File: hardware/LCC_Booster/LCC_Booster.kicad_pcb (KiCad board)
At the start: 2 copper layers, 115 x 100 mm, 101 parts, among them J1 A00-216-262-450, J2 54-00166, J3 Screw_Terminal_01x08, J4 Screw_Terminal_01x02, J5 Screw_Terminal_01x02, Q1 AO3400A, Q2 AO3400A, Q3 AO3400A, Q4 AO3400A, SW1 SW_Push, U1 ACPL-214-500E, U10 7410, U11 DRV8874PWPR, U12 7410, U13 7410, U14 7410, U15 7410, U16 DRV8874PWPR, U17 7410, U18 7410, U19 7410, U2 7410, U20 7410, U21 DRV8874PWPR, U22 MCP2518FD-xQBB, U23 MCP2562-E-SN, U3 7410, U4 7410, U5 7410, U6 DRV8874PWPR, U7 7410, U8 7410, U9 7410, Y1 ECS-400-20-46X

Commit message: Update to hardware v2 and cleanup
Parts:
- removed C36, C38, C41, C42, C43: C100n, Capacitor_SMD:C_0402_1005Metric_Pad0.74x0.62mm_HandSolder
- removed C37: C10u, Capacitor_SMD:C_1206_3216Metric_Pad1.33x1.80mm_HandSolder
- removed C39, C40: C22n, Capacitor_SMD:C_0402_1005Metric_Pad0.74x0.62mm_HandSolder
- removed C44, C45: C22p, Capacitor_SMD:C_0402_1005Metric_Pad0.74x0.62mm_HandSolder
- removed J4, J5: Screw_Terminal_01x02, TerminalBlock_Phoenix:TerminalBlock_Phoenix_MKDS-1,5-2_1x02_P5.00mm_Horizontal
- removed Q1, Q2, Q3, Q4: AO3400A, Package_TO_SOT_SMD:SOT-23
- removed U13, U14, U15, U17, U18, U19, U20: 7410, Package_SO:SOIC-14_3.9x8.7mm_P1.27mm
- removed U16, U21: DRV8874PWPR, DRV8874:PWP0016J_NV
- removed U22: MCP2518FD-xQBB, Package_SO:SOIC-14_3.9x8.7mm_P1.27mm
- removed U23: MCP2562-E-SN, Package_SO:SOIC-8_3.9x4.9mm_P1.27mm
- added JP6: SolderJumper_2_Bridged, Jumper:SolderJumper-2_P1.3mm_Bridged_RoundedPad1.0x1.5mm, F.Cu at (52.6, 74.0)
- added JP7: SolderJumper_2_Bridged, Jumper:SolderJumper-2_P1.3mm_Bridged_RoundedPad1.0x1.5mm, F.Cu at (52.6, 89.0)
- added JP8: SolderJumper_3_Bridged12, Jumper:SolderJumper-3_P1.3mm_Bridged12_RoundedPad1.0x1.5mm_NumberLabels, F.Cu at (91.0, 63.0)
- added JP9: SolderJumper_3_Bridged12, Jumper:SolderJumper-3_P1.3mm_Bridged12_RoundedPad1.0x1.5mm_NumberLabels, F.Cu at (87.0, 63.0)
- C10, C19, C9: value C22n -> C100n
- C11, C18, C25, C4: value C100n -> C10u; footprint Capacitor_SMD:C_0402_1005Metric_Pad0.74x0.62mm_HandSolder -> Capacitor_SMD:C_1206_3216Metric_Pad1.33x1.80mm_HandSolder
- C13, C14, C21, C28, C6: value C100n -> C22n
- C17: value C10u -> C100n; footprint Capacitor_SMD:C_1206_3216Metric_Pad1.33x1.80mm_HandSolder -> Capacitor_SMD:C_0402_1005Metric_Pad0.74x0.62mm_HandSolder
- C27, C7: value C10u -> C22n; footprint Capacitor_SMD:C_1206_3216Metric_Pad1.33x1.80mm_HandSolder -> Capacitor_SMD:C_0402_1005Metric_Pad0.74x0.62mm_HandSolder
- C29, C30: value C22n -> C22p
- J3: footprint TerminalBlock_Phoenix:TerminalBlock_Phoenix_MKDS-1,5-8_1x08_P5.00mm_Horizontal -> TerminalBlock_Phoenix:TerminalBlock_Phoenix_MKDS-1,5-12_1x12_P5.00mm_Horizontal
- JP1, JP3: value SolderJumper_3_Bridged12 -> SolderJumper_2_Open; footprint Jumper:SolderJumper-3_P1.3mm_Bridged12_RoundedPad1.0x1.5mm_NumberLabels -> Jumper:SolderJumper-2_P1.3mm_Open_RoundedPad1.0x1.5mm
- JP2: value SolderJumper_3_Bridged12 -> SolderJumper_2_Open; footprint Jumper:SolderJumper-3_P1.3mm_Bridged12_RoundedPad1.0x1.5mm_NumberLabels -> Jumper:SolderJumper-2_P1.3mm_Bridged_RoundedPad1.0x1.5mm
- JP4: value SolderJumper_3_Bridged12 -> SolderJumper_2_Bridged; footprint Jumper:SolderJumper-3_P1.3mm_Bridged12_RoundedPad1.0x1.5mm_NumberLabels -> Jumper:SolderJumper-2_P1.3mm_Bridged_RoundedPad1.0x1.5mm
- JP5: value SolderJumper_2_Open -> SolderJumper_2_Bridged; footprint Jumper:SolderJumper-2_P1.3mm_Open_RoundedPad1.0x1.5mm -> Jumper:SolderJumper-2_P1.3mm_Bridged_RoundedPad1.0x1.5mm
- U10, U4, U8: value 7410 -> DRV8874PWPR; footprint Package_SO:SOIC-14_3.9x8.7mm_P1.27mm -> DRV8874:PWP0016J_NV
- U11: value DRV8874PWPR -> MCP2518FD-xQBB; footprint DRV8874:PWP0016J_NV -> Package_SO:SOIC-14_3.9x8.7mm_P1.27mm
- U12: value 7410 -> MCP2562-E-SN; footprint Package_SO:SOIC-14_3.9x8.7mm_P1.27mm -> Package_SO:SOIC-8_3.9x4.9mm_P1.27mm
- U2: value 7410 -> ACPL-214-500E; footprint Package_SO:SOIC-14_3.9x8.7mm_P1.27mm -> Package_SO:SOP-4_4.4x2.6mm_P1.27mm
- U3, U5, U7, U9: value 7410 -> SN74HC253DR; footprint Package_SO:SOIC-14_3.9x8.7mm_P1.27mm -> Package_SO:SO-16_3.9x9.9mm_P1.27mm
- moved H2 106.3 mm to (100.0, 30.0)
- moved H4 106.3 mm to (30.0, 110.0)
- moved JP5 75.1 mm to (52.6, 59.0)
- moved U2 72.0 mm to (83.0, 98.0), turned to 90 degrees
- moved C30 65.9 mm to (108.9, 70.3), turned to 90 degrees
- moved U11 63.6 mm to (103.0, 62.0), turned to 90 degrees
- moved C29 61.8 mm to (101.0, 70.3), turned to 90 degrees
- moved JP4 57.9 mm to (52.6, 44.0), turned to 90 degrees
- moved SW1 57.1 mm to (66.5, 36.0), turned to 90 degrees
- moved C32 55.2 mm to (97.0, 59.5), turned to 180 degrees
- moved C31 50.2 mm to (86.5, 75.5), turned to 180 degrees
- moved R10 49.9 mm to (43.7, 87.5), turned to 180 degrees
- moved C33 49.2 mm to (80.5, 72.0), turned to 90 degrees
- moved U1 46.9 mm to (83.0, 85.0)
- moved U9 45.2 mm to (52.7, 94.6), turned to -90 degrees
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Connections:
- A1 pad 1: /dcc_en_D -> /dcc_en_C
- A1 pad 12: /pwm_B -> /pwm_A
- A1 pad 19: /sense_A -> /sense_D
- A1 pad 2: /dcc_en_C -> /dcc_en_D
- A1 pad 20: /sense_B -> /sense_C
- A1 pad 21: /sense_C -> /sense_B
- A1 pad 22: /sense_D -> /sense_A
- A1 pad 25: /dcc_en_A -> /dcc_en_B
- A1 pad 26: /dcc_en_B -> /dcc_en_A
- A1 pad 6: /pwm_A -> /pwm_D
- A1 pad 8: /pwm_D -> /pwm_C
- A1 pad 9: /pwm_C -> /pwm_B
- C10 pad 1: /sense_A -> VTRACK
- C10 pad 2: GND -> Net-(U6-VCP)
- C11 pad 1: IOREF -> VTRACK
- C12 pad 1: IOREF -> VTRACK
- C13 pad 1: IOREF -> Net-(U6-CPH)
- C13 pad 2: GND -> Net-(U6-CPL)
- C14 pad 1: IOREF -> /sense_B
- C16 pad 1: VTRACK -> IOREF
- C16 pad 2: Net-(U11-VCP) -> GND
- C17 pad 2: GND -> Net-(U8-VCP)
- C19 pad 1: Net-(U11-CPH) -> VTRACK
- C19 pad 2: Net-(U11-CPL) -> GND
- C20 pad 1: /sense_B -> Net-(U8-CPH)
- C20 pad 2: GND -> Net-(U8-CPL)
- C21 pad 1: IOREF -> /sense_C
- C24 pad 1: IOREF -> VTRACK
- C24 pad 2: GND -> Net-(U10-VCP)
- C25 pad 1: IOREF -> VTRACK
- C26 pad 2: Net-(U16-VCP) -> GND
- C27 pad 1: VTRACK -> Net-(U10-CPH)
- C27 pad 2: GND -> Net-(U10-CPL)
- C28 pad 1: VTRACK -> /sense_D
- C29 pad 1: Net-(U16-CPH) -> GND
- C29 pad 2: Net-(U16-CPL) -> Net-(U11-OSC2)
- C3 pad 1: IOREF -> VTRACK
- C3 pad 2: GND -> Net-(U4-VCP)
- C30 pad 1: /sense_C -> GND
- C30 pad 2: GND -> Net-(U11-OSC1)
- C33 pad 1: IOREF -> +5V
- C4 pad 1: IOREF -> VTRACK
- C5 pad 1: IOREF -> VTRACK
- C6 pad 1: VTRACK -> Net-(U4-CPH)
- C6 pad 2: Net-(U6-VCP) -> Net-(U4-CPL)
- C7 pad 1: VTRACK -> /sense_A
- C8 pad 1: VTRACK -> IOREF
- C9 pad 1: Net-(U6-CPH) -> IOREF
- C9 pad 2: Net-(U6-CPL) -> GND
- J3 pad 1: /out2_D -> /raw_dcc_n
- J3 pad 2: /out1_D -> /raw_dcc_p
- J3 pad 3: /out2_C -> /out2_D
- J3 pad 4: /out1_C -> /out1_D
- J3 pad 5: /out2_B -> /out2_C
- J3 pad 6: /out1_B -> /out1_C
- J3 pad 7: /out2_A -> /out2_B
- J3 pad 8: /out1_A -> /out1_B
- JP1 pad 1: +5V -> /can_shield
- JP1 pad 2: 3v3_IOREF -> GND
- JP3 pad 1: Net-(JP3-A) -> IOREF
- JP3 pad 2: /cs_canrx -> +5V
- JP4 pad 1: Net-(JP4-A) -> GND
- JP4 pad 2: /int_cantx -> Net-(JP4-B)
- JP5 pad 1: /can_shield -> GND
- JP5 pad 2: GND -> Net-(JP5-B)
- R1 pad 2: Net-(U6-FAULT_N) -> Net-(U4-FAULT_N)
- R10 pad 2: Net-(U21-FAULT_N) -> Net-(U10-FAULT_N)
- R2 pad 2: Net-(Q1-D) -> Net-(JP4-B)
- R3 pad 1: Net-(Q1-D) -> Net-(JP4-B)
- R4 pad 2: Net-(U11-FAULT_N) -> Net-(U6-FAULT_N)
- R5 pad 2: Net-(Q2-D) -> Net-(JP5-B)
- R6 pad 1: Net-(Q2-D) -> Net-(JP5-B)
- R7 pad 2: Net-(U16-FAULT_N) -> Net-(U8-FAULT_N)
- U10 pad 1: Net-(U10-Pad1) -> Net-(U10-EN_IN1)
- U10 pad 10: unconnected-(U10-Pad10) -> /out2_D
- U10 pad 11: unconnected-(U10-Pad11) -> VTRACK
- U10 pad 12: Net-(U11-EN_IN1) -> Net-(U10-VCP)
- U10 pad 13: Net-(U10-Pad13) -> Net-(U10-CPH)
- U10 pad 14: IOREF -> Net-(U10-CPL)
- U10 pad 2: Net-(U10-Pad2) -> Net-(U10-PH_IN2)
- U10 pad 3: Net-(U10-Pad3) -> IOREF
- U10 pad 4: Net-(U10-Pad4) -> Net-(U10-FAULT_N)
- U10 pad 5: Net-(U10-Pad5) -> IOREF
- U10 pad 6: Net-(U11-PH_IN2) -> /sense_D
- U10 pad 8: unconnected-(U10-Pad8) -> /out1_D
- U10 pad 9: unconnected-(U10-Pad9) -> GND
- U11 pad 1: Net-(U11-EN_IN1) -> Net-(JP9-B)
- U11 pad 10: /out2_B -> /sck
- U11 pad 11: VTRACK -> /copi
- U11 pad 12: Net-(U11-VCP) -> /cipo
- U11 pad 13: Net-(U11-CPH) -> Net-(JP8-A)
- U11 pad 14: Net-(U11-CPL) -> IOREF
- U11 pad 2: Net-(U11-PH_IN2) -> Net-(JP8-B)
- U11 pad 3: IOREF -> unconnected-(U11-CLKO/SOF-Pad3)
- U11 pad 4: Net-(U11-FAULT_N) -> Net-(JP9-A)
- U11 pad 5: IOREF -> Net-(U11-OSC2)
- U11 pad 6: /sense_B -> Net-(U11-OSC1)
- U11 pad 8: /out1_B -> unconnected-(U11-~{INT1}/GPIO1-Pad8)
- U11 pad 9: GND -> unconnected-(U11-~{INT0}/GPIO0/XSTBY-Pad9)
- U12 pad 1: /dcc_en_C -> Net-(JP9-B)
- U12 pad 2: /dcc_en_C -> GND
- U12 pad 3: /dir_C -> +5V
- U12 pad 4: /dir_C -> Net-(JP8-B)
- U12 pad 5: /dir_C -> IOREF
- U12 pad 6: Net-(U12-Pad6) -> /can_l
- U12 pad 7: GND -> /can_h
- U12 pad 8: Net-(U12-Pad8) -> GND
- U2 pad 1: /dcc_en_A -> /raw_dcc_n
- U2 pad 2: /dcc_en_A -> GND
- U2 pad 3: /dir_A -> /dcc_n
- U2 pad 4: /dir_A -> IOREF
- U3 pad 1: Net-(U2-Pad8) -> GND
- U3 pad 10: Net-(U2-Pad12) -> GND
- U3 pad 11: Net-(U2-Pad6) -> /pwm_A
- U3 pad 12: Net-(U3-Pad12) -> /dcc_n
- U3 pad 13: /dir_A -> /dcc_p
- U3 pad 14: IOREF -> /dir_A
- U3 pad 3: /dcc_p -> /dcc_n
- U3 pad 4: /dcc_en_A -> /dcc_p
- U3 pad 5: Net-(U2-Pad6) -> GND
- U3 pad 6: Net-(U3-Pad6) -> /pwm_A
- U3 pad 7: GND -> Net-(U3-1Y)
- U3 pad 8: Net-(U3-Pad8) -> GND
- U3 pad 9: /pwm_A -> Net-(U3-2Y)
- U4 pad 1: /dcc_p -> Net-(U3-1Y)
- U4 pad 10: Net-(U2-Pad12) -> /out2_A
- U4 pad 11: /dir_A -> VTRACK
- U4 pad 12: Net-(U4-Pad12) -> Net-(U4-VCP)
- U4 pad 13: /dir_A -> Net-(U4-CPH)
- U4 pad 14: IOREF -> Net-(U4-CPL)
- U4 pad 2: /dcc_en_A -> Net-(U3-2Y)
- U4 pad 3: Net-(U2-Pad8) -> IOREF
- U4 pad 4: /dcc_en_A -> Net-(U4-FAULT_N)
- U4 pad 5: Net-(U2-Pad6) -> IOREF
- U4 pad 6: Net-(U4-Pad6) -> /sense_A
- U4 pad 8: Net-(U4-Pad8) -> /out1_A
- U4 pad 9: /pwm_A -> GND
- U5 pad 1: Net-(U3-Pad12) -> GND
- U5 pad 10: unconnected-(U5-Pad10) -> GND
- U5 pad 11: unconnected-(U5-Pad11) -> /pwm_B
- U5 pad 12: Net-(U6-EN_IN1) -> /dcc_n
- U5 pad 13: Net-(U3-Pad8) -> /dcc_p
- U5 pad 14: IOREF -> /dir_B
- U5 pad 2: Net-(U3-Pad6) -> /dcc_en_B
- U5 pad 3: Net-(U4-Pad12) -> /dcc_n
- U5 pad 4: Net-(U4-Pad6) -> /dcc_p
- U5 pad 5: Net-(U4-Pad8) -> GND
- U5 pad 6: Net-(U6-PH_IN2) -> /pwm_B
- U5 pad 7: GND -> Net-(U5-1Y)
- U5 pad 8: unconnected-(U5-Pad8) -> GND
- U5 pad 9: unconnected-(U5-Pad9) -> Net-(U5-2Y)
- U6 pad 1: Net-(U6-EN_IN1) -> Net-(U5-1Y)
- U6 pad 10: /out2_A -> /out2_B
- U6 pad 2: Net-(U6-PH_IN2) -> Net-(U5-2Y)
- U6 pad 6: /sense_A -> /sense_B
- U6 pad 8: /out1_A -> /out1_B
- U7 pad 1: /dcc_en_B -> GND
- U7 pad 10: /dcc_p -> GND
- U7 pad 11: /dcc_p -> /pwm_C
- U7 pad 12: Net-(U7-Pad12) -> /dcc_n
- U7 pad 13: /dcc_en_B -> /dcc_p
- U7 pad 14: IOREF -> /dir_C
- U7 pad 2: /dcc_en_B -> /dcc_en_C
- U7 pad 3: /dir_B -> /dcc_n
- U7 pad 4: /dir_B -> /dcc_p
- U7 pad 5: /dir_B -> GND
- U7 pad 6: Net-(U7-Pad6) -> /pwm_C
- U7 pad 7: GND -> Net-(U7-1Y)
- U7 pad 8: Net-(U7-Pad8) -> GND
- U7 pad 9: /dcc_p -> Net-(U7-2Y)
- U8 pad 1: Net-(U7-Pad8) -> Net-(U7-1Y)
- U8 pad 10: Net-(U7-Pad12) -> /out2_C
- U8 pad 11: Net-(U7-Pad6) -> VTRACK
- U8 pad 12: Net-(U10-Pad1) -> Net-(U8-VCP)
- U8 pad 13: /dir_B -> Net-(U8-CPH)
- U8 pad 14: IOREF -> Net-(U8-CPL)
- U8 pad 2: /dcc_en_B -> Net-(U7-2Y)
- U8 pad 3: /dcc_p -> IOREF
- U8 pad 4: /dcc_en_B -> Net-(U8-FAULT_N)
- U8 pad 5: Net-(U7-Pad6) -> IOREF
- U8 pad 6: Net-(U10-Pad2) -> /sense_C
- U8 pad 8: Net-(U10-Pad13) -> /out1_C
- U8 pad 9: /pwm_B -> GND
- U9 pad 1: /dcc_p -> GND
- U9 pad 10: Net-(U7-Pad12) -> GND
- U9 pad 11: /dir_B -> /pwm_D
- U9 pad 12: Net-(U10-Pad3) -> /dcc_n
- U9 pad 13: /dir_B -> /dcc_p
- U9 pad 14: IOREF -> /dir_D
- U9 pad 2: /dcc_en_B -> /dcc_en_D
- U9 pad 3: Net-(U7-Pad8) -> /dcc_n
- U9 pad 4: /dcc_en_B -> /dcc_p
- U9 pad 5: Net-(U7-Pad6) -> GND
- U9 pad 6: Net-(U10-Pad4) -> /pwm_D
- U9 pad 7: GND -> Net-(U10-EN_IN1)
- U9 pad 8: Net-(U10-Pad5) -> GND
- U9 pad 9: /pwm_B -> Net-(U10-PH_IN2)
- Y1 pad 1: Net-(U22-OSC1) -> Net-(U11-OSC1)
- Y1 pad 2: Net-(U22-OSC2) -> Net-(U11-OSC2)
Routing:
- net IOREF: track 575.4 -> 267.0 mm, vias 20 -> 18
- net 3v3_IOREF: track 148.3 -> 0.00 mm, vias 4 -> 0
- net /dcc_n: track 0.00 -> 125.4 mm, vias 0 -> 5
- net /raw_dcc_p: track 197.2 -> 100.5 mm
- net /dcc_p: track 240.7 -> 147.6 mm, vias 8 -> 5
- net /sense_D: track 171.2 -> 94.9 mm, vias 3 -> 0
- net GND: track 412.6 -> 350.7 mm, vias 130 -> 66
- net /dir_D: track 114.2 -> 53.9 mm, vias 5 -> 2
- net Net-(U21-FAULT_N): track 59.7 -> 0.00 mm
- net /dcc_en_D: track 96.7 -> 42.9 mm, vias 2 -> 0
- net /sense_C: track 132.0 -> 79.6 mm, vias 2 -> 0
- net Net-(U11-FAULT_N): track 50.0 -> 0.00 mm, vias 2 -> 0
- net +5V: track 108.2 -> 58.6 mm
- net /dcc_en_C: track 79.4 -> 29.8 mm, vias 2 -> 0
- net /sense_A: track 110.1 -> 62.1 mm
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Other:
- board size 115 x 100 mm -> 90 x 100 mm
- board text added: "3.3v"
- board text added: "5v"
- board text added: "Nano V_{IN}"
- board text added: "Reset"
- board text added: "TMRC System 4 Block Card v2"
- board text added: "V_{TRACK}"
- board text removed: "3.3V"
- board text removed: "5V"
- board text removed: "CAN"
- board text removed: "RESET"
- board text removed: "SPI"
- board text removed: "TMRC System 4 Block Card v1.0"
- board text removed: "V_TRACK"

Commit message: Update Schematic
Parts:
- added R13: R1k 2W, Resistor_SMD:R_01005_0402Metric_Pad0.57x0.30mm_HandSolder, F.Cu at (64.8, 98.2)
- added R14: R10k, Resistor_SMD:R_01005_0402Metric_Pad0.57x0.30mm_HandSolder, F.Cu at (85.0, 85.8)
- added R15: R10k, Resistor_SMD:R_01005_0402Metric_Pad0.57x0.30mm_HandSolder, F.Cu at (79.5, 99.2)
- U1, U2: value ACPL-214-500E -> 6N137; footprint Package_SO:SOP-4_4.4x2.6mm_P1.27mm -> Package_DIP:DIP-8_W7.62mm_SMDSocket_SmallPads
- moved U1 17.7 mm to (72.5, 99.2), turned to 0 degrees
- moved U2 14.5 mm to (78.2, 84.2), turned to 0 degrees
- moved C34 4.78 mm to (83.5, 78.2), turned to 0 degrees
- moved C35 2.57 mm to (77.8, 93.2), turned to 0 degrees
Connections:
- C34 pad 1: IOREF -> +5V
- C35 pad 1: IOREF -> +5V
- U1 pad 1: /raw_dcc_p -> unconnected-(U1-NC-Pad1)
- U1 pad 2: GND -> Net-(U1-A)
- U1 pad 3: /dcc_p -> /raw_dcc_n
- U1 pad 4: IOREF -> unconnected-(U1-NC-Pad4)
- U2 pad 1: /raw_dcc_n -> unconnected-(U2-NC-Pad1)
- U2 pad 2: GND -> /raw_dcc_n
- U2 pad 3: /dcc_n -> Net-(U1-A)
- U2 pad 4: IOREF -> unconnected-(U2-NC-Pad4)
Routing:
- net /raw_dcc_n: track 94.8 -> 129.9 mm
- net +5V: track 58.6 -> 89.0 mm
- net GND: track 350.7 -> 379.8 mm
- net Net-(U1-A): track 0.00 -> 22.0 mm
- net /raw_dcc_p: track 100.5 -> 111.5 mm
- net /dcc_n: track 125.4 -> 116.6 mm
- net /dcc_p: track 147.6 -> 152.1 mm, vias 5 -> 6
- net IOREF: track 267.0 -> 271.3 mm
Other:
- board text added: "TMRC System 4 Block Card v3"
- board text removed: "TMRC System 4 Block Card v2"

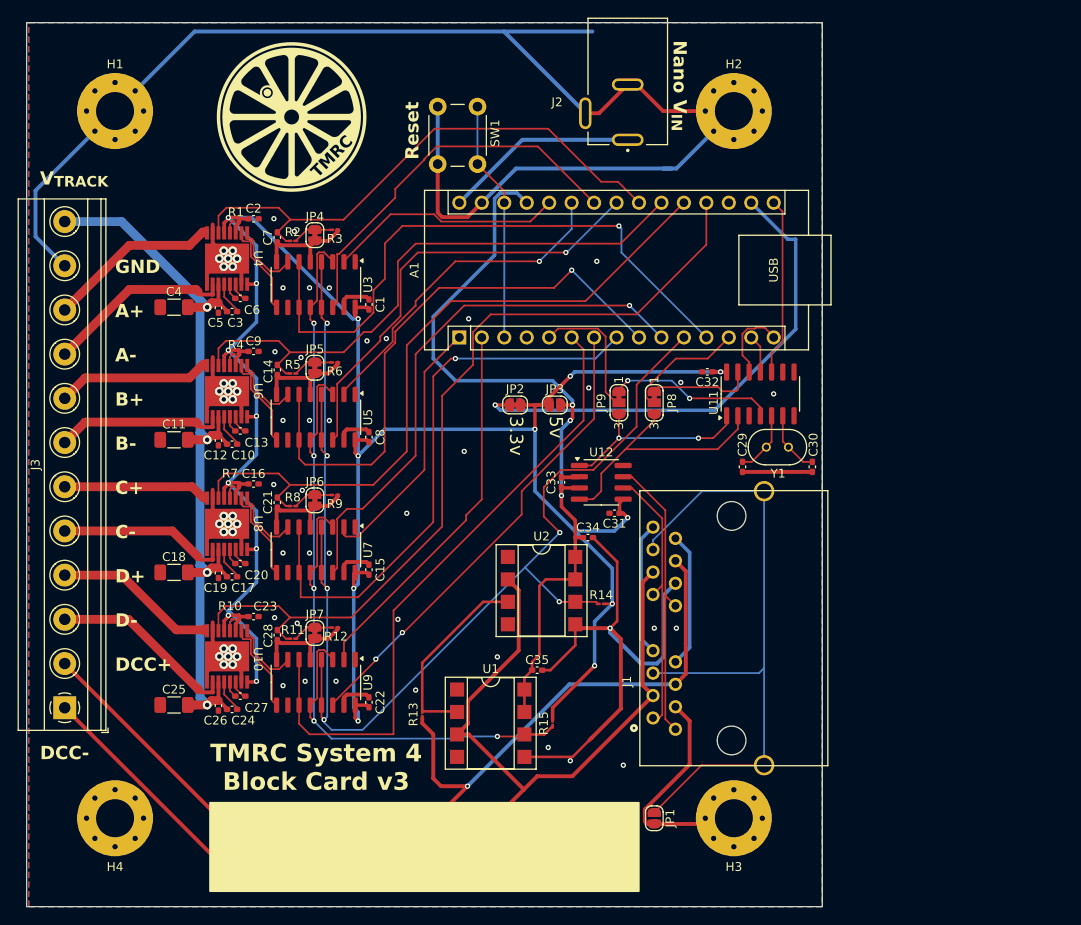
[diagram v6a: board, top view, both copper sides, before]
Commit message: Add Fault Pin Inputs to Arduino
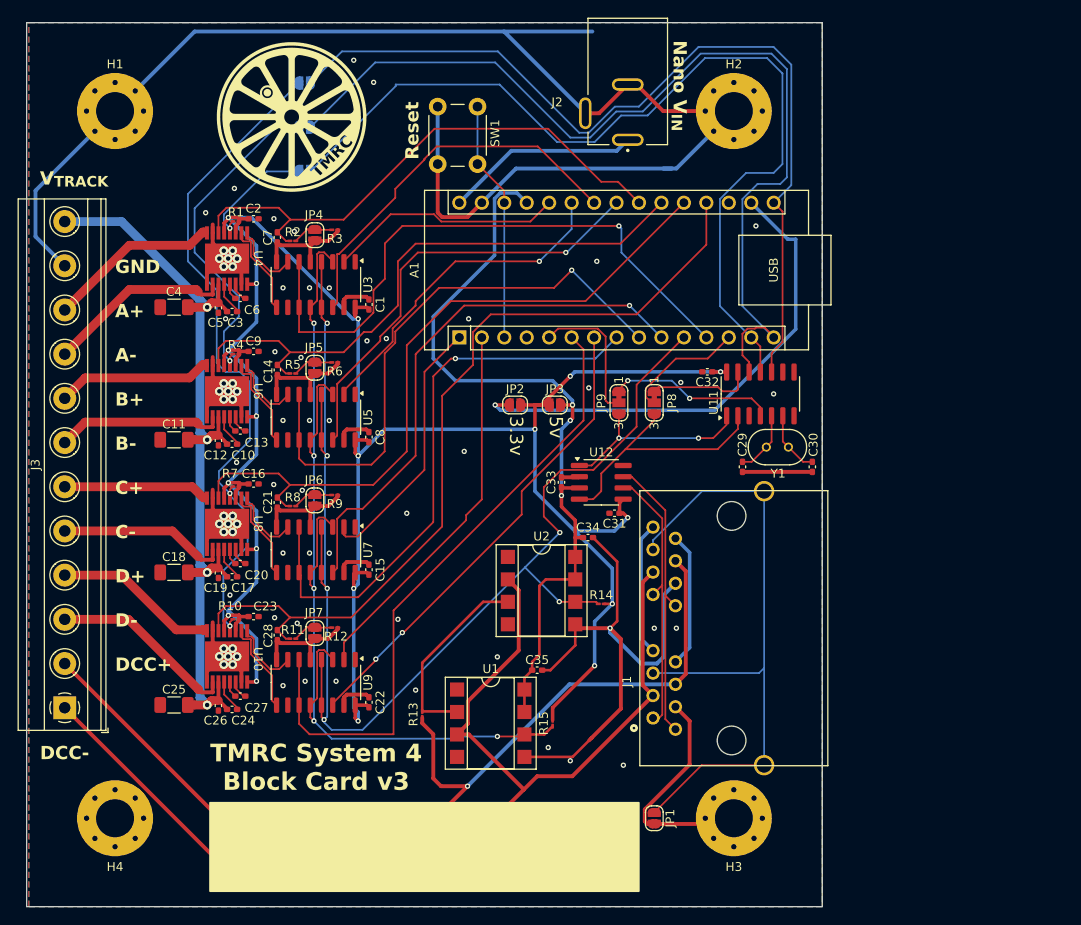
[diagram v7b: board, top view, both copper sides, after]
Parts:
- added JP10: SolderJumper_2_Open, Jumper:SolderJumper-2_P1.3mm_Open_RoundedPad1.0x1.5mm, B.Cu at (51.4, 36.8)
- added JP11: SolderJumper_2_Open, Jumper:SolderJumper-2_P1.3mm_Open_RoundedPad1.0x1.5mm, B.Cu at (51.4, 31.8)
- added JP12: SolderJumper_2_Open, Jumper:SolderJumper-2_P1.3mm_Open_RoundedPad1.0x1.5mm, B.Cu at (51.4, 26.8)
- JP2: footprint Jumper:SolderJumper-2_P1.3mm_Bridged_RoundedPad1.0x1.5mm -> Jumper:SolderJumper-2_P1.3mm_Open_RoundedPad1.0x1.5mm
- JP4, JP5, JP6, JP7: value SolderJumper_2_Bridged -> SolderJumper_2; footprint Jumper:SolderJumper-2_P1.3mm_Bridged_RoundedPad1.0x1.5mm -> Jumper:SolderJumper-2_P1.3mm_Open_RoundedPad1.0x1.5mm
- R11, R2, R5, R8: value R1k43 -> R1k430
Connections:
- net /cipo renamed /cipo-nFault_B
- net /copi renamed /copi-nFault_A
- net /cs_canrx renamed /cs-canrx
- net /int_cantx renamed /int-cantx
- net /sck renamed /sck-nFault_CD
- net Net-(U4-FAULT_N) renamed /nFault_A
- net Net-(U6-FAULT_N) renamed /nFault_B
- R10 pad 2: Net-(U10-FAULT_N) -> /nFault_C
- R7 pad 2: Net-(U8-FAULT_N) -> /nFault_C
- U10 pad 4: Net-(U10-FAULT_N) -> /nFault_C
- U8 pad 4: Net-(U8-FAULT_N) -> /nFault_C
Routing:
- net /copi-nFault_A: track 4.34 -> 105.4 mm
- net /cipo-nFault_B: track 8.99 -> 109.5 mm
- net /sck-nFault_CD: track 20.1 -> 101.1 mm
- net /nFault_C: track 0.00 -> 77.6 mm, vias 0 -> 2
- net /nFault_B: track 1.44 -> 37.3 mm, vias 0 -> 1
- net /nFault_A: track 1.44 -> 13.8 mm, vias 0 -> 1
- net Net-(U8-FAULT_N): track 1.44 -> 0.00 mm
- net Net-(U10-FAULT_N): track 1.44 -> 0.00 mm
- net /int-cantx: track 15.5 -> 16.0 mm
- net GND: vias 66 -> 74

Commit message: Fix Some Hardware Pin Notations
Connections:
- A1 pad 3: /~{reset} -> unconnected-(A1-~{RESET}-Pad3)
- H1 pad 1: GND -> unconnected-(H1-Pad1)_2
- H2 pad 1: GND -> unconnected-(H2-Pad1)_4
- H3 pad 1: GND -> unconnected-(H3-Pad1)_2
- H4 pad 1: GND -> unconnected-(H4-Pad1)_6
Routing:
- net GND: track 379.8 -> 324.3 mm
- net /~{reset}: track 27.4 -> 12.1 mm
- net /sck-nFault_CD: track 101.1 -> 93.5 mm
- net /cipo-nFault_B: track 109.5 -> 102.5 mm
- net /copi-nFault_A: track 105.4 -> 100.3 mm
- net unconnected-(H3-Pad1)_8: track 0.00 -> 0.92 mm
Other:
- board text added: "+3.3V"
- board text added: "+5V"
- board text added: "TMRC System 4 Block Card v4"
- board text added: "VIN"
- board text removed: "TMRC System 4 Block Card v3"
